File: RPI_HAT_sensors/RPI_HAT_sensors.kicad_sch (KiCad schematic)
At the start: 39 parts, among them J5 Conn_01x01, J6 Conn_01x01

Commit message: h
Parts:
- RV1, RV2: value R_Potentiometer -> 10k
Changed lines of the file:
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@@
     (pin "1")
   )
-  (symbol (lib_id "Connector_Generic:Conn_01x01") (at 355.6 128.27 270) (unit 1)
-    (in_bom yes) (on_board yes) (fields_autoplaced)
-    (property "Reference" "J5" (id 0) (at 358.14 126.9999 90)
-      (effects (font (size 1.27 1.27)) (justify left))
-    )
-    (property "Value" "Conn_01x01" (id 1) (at 358.14 129.5399 90)
-      (effects (font (size 1.27 1.27)) (justify left))
-    )
-    (property "Footprint" "Connector_PinHeader_2.54mm:PinHeader_1x01_P2.54mm_Vertical" (id 2) (at 355.6 128.27 0)
-      (effects (font (size 1.27 1.27)) hide)
-    )
-    (property "Datasheet" "~" (id 3) (at 355.6 128.27 0)
-      (effects (font (size 1.27 1.27)) hide)
-    )
-    (pin "1")
-  )
-  (symbol (lib_id "Device:R_Potentiometer") (at 358.14 77.47 0) (unit 1)
-    (in_bom yes) (on_board yes) (fields_autoplaced)
-    (property "Reference" "RV3" (id 0) (at 355.6 76.1999 0)
-      (effects (font (size 1.27 1.27)) (justify right))
-    )
-    (property "Value" "" (id 1) (at 355.6 78.7399 0)
-      (effects (font (size 1.27 1.27)) (justify right))
-    )
-    (property "Footprint" "" (id 2) (at 358.14 77.47 0)
-      (effects (font (size 1.27 1.27)) hide)
-    )
-    (property "Datasheet" "~" (id 3) (at 358.14 77.47 0)
+  (symbol (lib_id "Device:R_Potentiometer") (at 355.6 116.84 0) (unit 1)
+    (in_bom yes) (on_board yes) (fields_autoplaced)
+    (property "Reference" "RV2" (id 0) (at 353.06 115.5699 0)
+      (effects (font (size 1.27 1.27)) (justify right))
+    )
+    (property "Value" "10k" (id 1) (at 353.06 118.1099 0)
+      (effects (font (size 1.27 1.27)) (justify right))
+    )
+    (property "Footprint" "" (id 2) (at 355.6 116.84 0)
+      (effects (font (size 1.27 1.27)) hide)
+    )
+    (property "Datasheet" "~" (id 3) (at 355.6 116.84 0)
       (effects (font (size 1.27 1.27)) hide)
     )
@@
     (pin "3")
   )
-  (symbol (lib_id "Connector_Generic:Conn_01x01") (at 290.83 128.27 270) (unit 1)
-    (in_bom yes) (on_board yes) (fields_autoplaced)
-    (property "Reference" "J4" (id 0) (at 293.37 126.9999 90)
-      (effects (font (size 1.27 1.27)) (justify left))
-    )
-    (property "Value" "" (id 1) (at 293.37 129.5399 90)
-      (effects (font (size 1.27 1.27)) (justify left))
-    )
-    (property "Footprint" "" (id 2) (at 290.83 128.27 0)
-      (effects (font (size 1.27 1.27)) hide)
-    )
-    (property "Datasheet" "~" (id 3) (at 290.83 128.27 0)
-      (effects (font (size 1.27 1.27)) hide)
-    )
-    (pin "1")
-  )
-  (symbol (lib_id "Device:R_Potentiometer") (at 290.83 116.84 0) (unit 1)
-    (in_bom yes) (on_board yes) (fields_autoplaced)
-    (property "Reference" "RV1" (id 0) (at 288.29 115.5699 0)
-      (effects (font (size 1.27 1.27)) (justify right))
-    )
-    (property "Value" "R_Potentiometer" (id 1) (at 288.29 118.1099 0)
-      (effects (font (size 1.27 1.27)) (justify right))
-    )
-    (property "Footprint" "" (id 2) (at 290.83 116.84 0)
-      (effects (font (size 1.27 1.27)) hide)
-    )
-    (property "Datasheet" "~" (id 3) (at 290.83 116.84 0)
+  (symbol (lib_id "Connector_Generic:Conn_01x01") (at 355.6 128.27 270) (unit 1)
+    (in_bom yes) (on_board yes) (fields_autoplaced)
+    (property "Reference" "J5" (id 0) (at 358.14 126.9999 90)
+      (effects (font (size 1.27 1.27)) (justify left))
+    )
+    (property "Value" "Conn_01x01" (id 1) (at 358.14 129.5399 90)
+      (effects (font (size 1.27 1.27)) (justify left))
+    )
+    (property "Footprint" "Connector_PinHeader_2.54mm:PinHeader_1x01_P2.54mm_Vertical" (id 2) (at 355.6 128.27 0)
+      (effects (font (size 1.27 1.27)) hide)
+    )
+    (property "Datasheet" "~" (id 3) (at 355.6 128.27 0)
+      (effects (font (size 1.27 1.27)) hide)
+    )
+    (pin "1")
+  )
+  (symbol (lib_id "Device:R_Potentiometer") (at 358.14 77.47 0) (unit 1)
+    (in_bom yes) (on_board yes) (fields_autoplaced)
+    (property "Reference" "RV3" (id 0) (at 355.6 76.1999 0)
+      (effects (font (size 1.27 1.27)) (justify right))
+    )
+    (property "Value" "" (id 1) (at 355.6 78.7399 0)
+      (effects (font (size 1.27 1.27)) (justify right))
+    )
+    (property "Footprint" "" (id 2) (at 358.14 77.47 0)
+      (effects (font (size 1.27 1.27)) hide)
+    )
+    (property "Datasheet" "~" (id 3) (at 358.14 77.47 0)
       (effects (font (size 1.27 1.27)) hide)
     )
@@
     (pin "3")
   )
-  (symbol (lib_id "Device:R_Potentiometer") (at 355.6 116.84 0) (unit 1)
-    (in_bom yes) (on_board yes) (fields_autoplaced)
-    (property "Reference" "RV2" (id 0) (at 353.06 115.5699 0)
-      (effects (font (size 1.27 1.27)) (justify right))
-    )
-    (property "Value" "R_Potentiometer" (id 1) (at 353.06 118.1099 0)
-      (effects (font (size 1.27 1.27)) (justify right))
-    )
-    (property "Footprint" "" (id 2) (at 355.6 116.84 0)
-      (effects (font (size 1.27 1.27)) hide)
-    )
-    (property "Datasheet" "~" (id 3) (at 355.6 116.84 0)
+  (symbol (lib_id "Connector_Generic:Conn_01x01") (at 290.83 128.27 270) (unit 1)
+    (in_bom yes) (on_board yes) (fields_autoplaced)
+    (property "Reference" "J4" (id 0) (at 293.37 126.9999 90)
+      (effects (font (size 1.27 1.27)) (justify left))
+    )
+    (property "Value" "" (id 1) (at 293.37 129.5399 90)
+      (effects (font (size 1.27 1.27)) (justify left))
+    )
+    (property "Footprint" "" (id 2) (at 290.83 128.27 0)
+      (effects (font (size 1.27 1.27)) hide)
+    )
+    (property "Datasheet" "~" (id 3) (at 290.83 128.27 0)
+      (effects (font (size 1.27 1.27)) hide)
+    )
+    (pin "1")
+  )
+  (symbol (lib_id "Device:R_Potentiometer") (at 290.83 116.84 0) (unit 1)
+    (in_bom yes) (on_board yes) (fields_autoplaced)
+    (property "Reference" "RV1" (id 0) (at 288.29 115.5699 0)
+      (effects (font (size 1.27 1.27)) (justify right))
+    )
+    (property "Value" "10k" (id 1) (at 288.29 118.1099 0)
+      (effects (font (size 1.27 1.27)) (justify right))
+    )
+    (property "Footprint" "" (id 2) (at 290.83 116.84 0)
+      (effects (font (size 1.27 1.27)) hide)
+    )
+    (property "Datasheet" "~" (id 3) (at 290.83 116.84 0)
       (effects (font (size 1.27 1.27)) hide)
     )
@@
       (reference "R8") (unit 1) (value "3K9") (footprint "Resistor_THT:R_Axial_DIN0204_L3.6mm_D1.6mm_P7.62mm_Horizontal")
     )
-    (path "/ebc401f4-0099-4bec-9a16-490c89dccf91"
-      (reference "RV1") (unit 1) (value "R_Potentiometer") (footprint "")
-    )
-    (path "/f263053c-853e-4bd4-bc1a-6c9983651d47"
-      (reference "RV2") (unit 1) (value "R_Potentiometer") (footprint "")
+    (path "/f4145bdb-e374-4b1f-80c3-57ff67cbefcd"
+      (reference "RV1") (unit 1) (value "10k") (footprint "")
+    )
+    (path "/99095c67-dbe4-40ff-b564-d4764560ce26"
+      (reference "RV2") (unit 1) (value "10k") (footprint "")
     )
     (path "/ae545ba3-9447-46ee-95c9-5c85b1932c57"
-      (reference "RV3") (unit 1) (value "R_Potentiometer") (footprint "")
+      (reference "RV3") (unit 1) (value "10k") (footprint "")
     )
     (path "/00000000-0000-0000-0000-000061c1d53c"

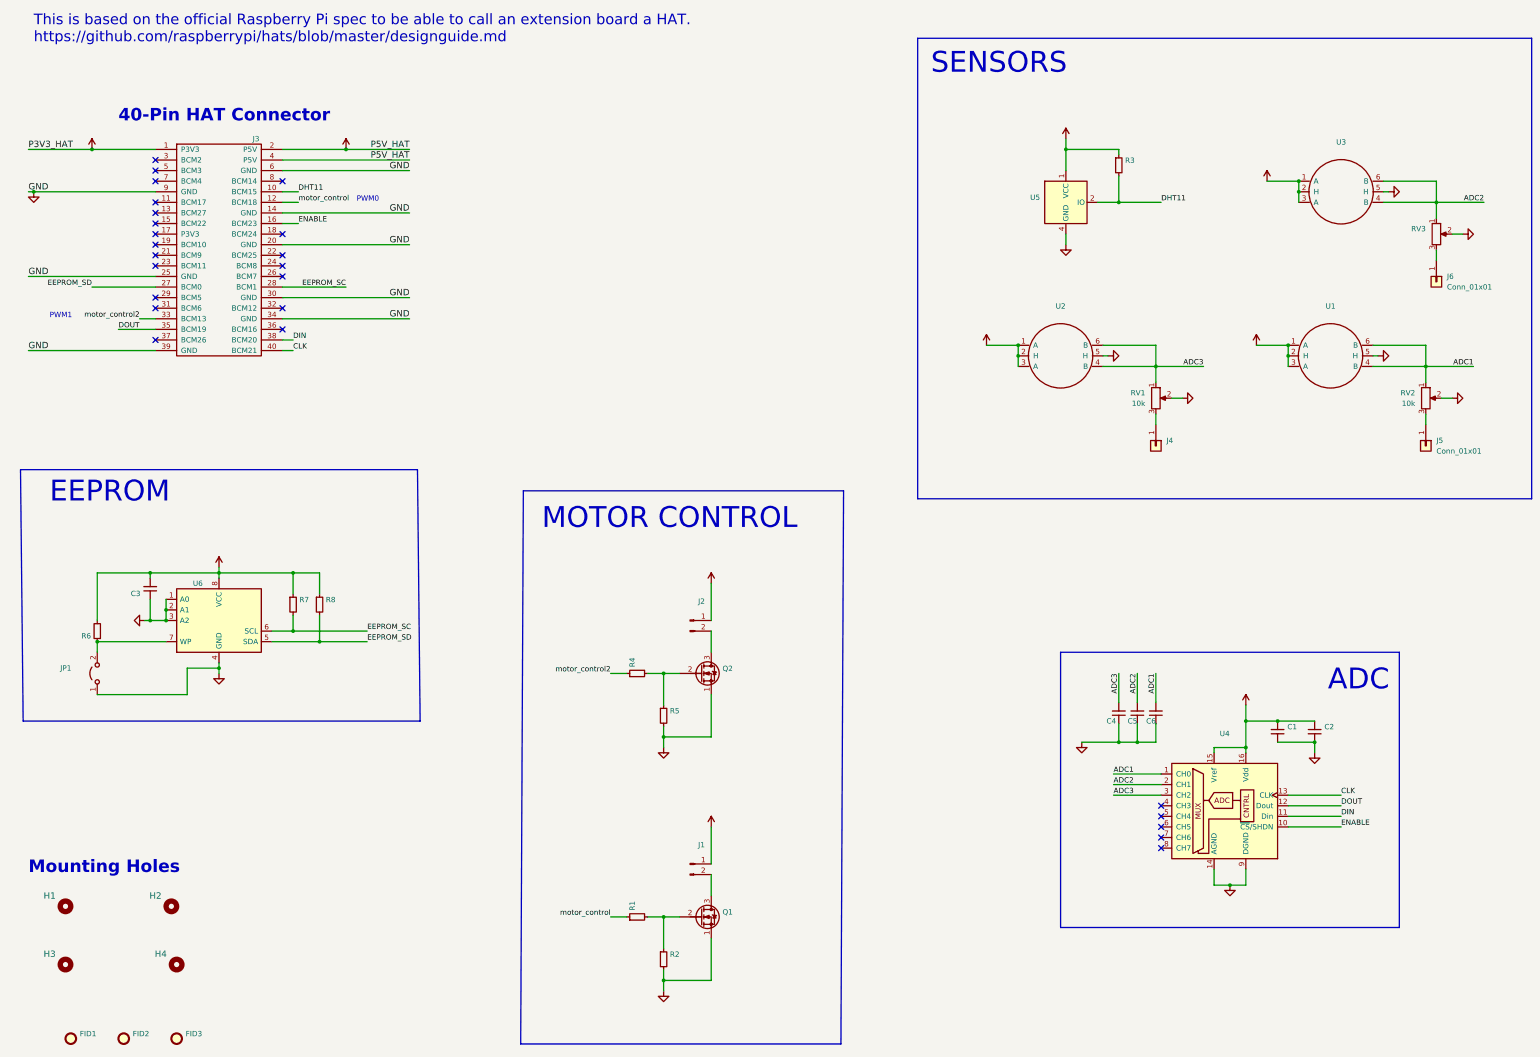
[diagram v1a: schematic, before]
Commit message: Update RPI_HAT_sensors.kicad_sch
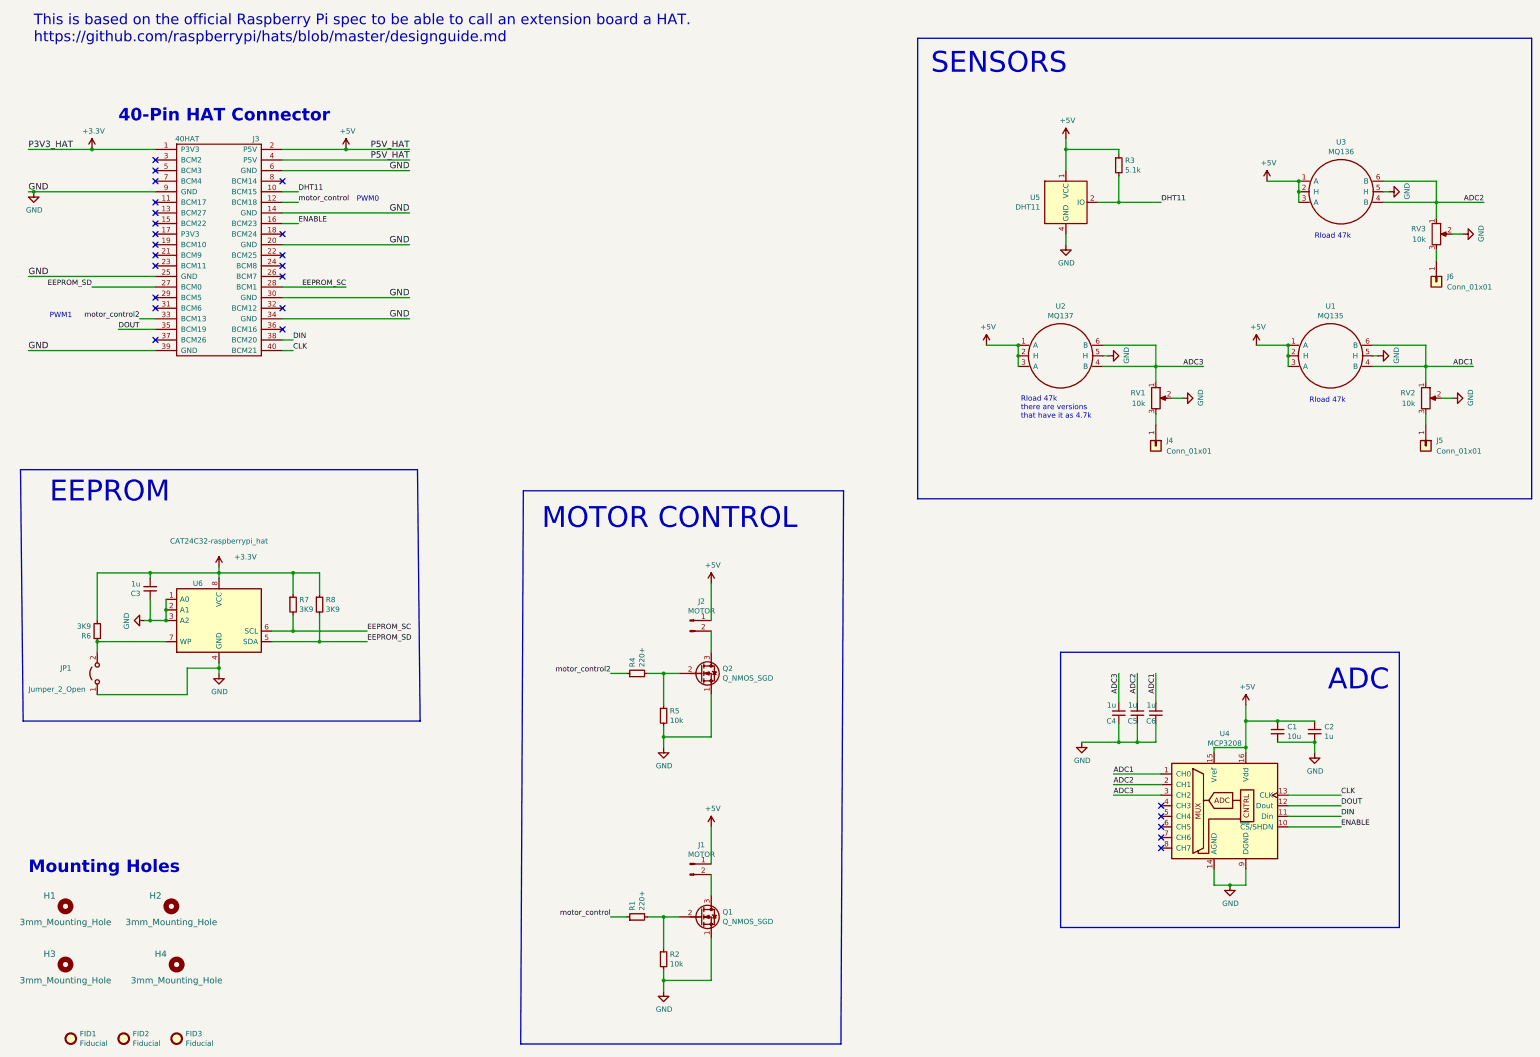
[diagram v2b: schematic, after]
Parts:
- C1: value (none) -> 10u; footprint (none) -> Capacitor_THT:C_Disc_D5.1mm_W3.2mm_P5.00mm
- C2, C3: value (none) -> 1u; footprint (none) -> Capacitor_THT:C_Disc_D5.1mm_W3.2mm_P5.00mm
- C4, C5, C6: value (none) -> 1u; footprint (none) -> Capacitor_SMD:C_0805_2012Metric_Pad1.15x1.40mm_HandSolder
- FID1, FID2, FID3: value (none) -> Fiducial; footprint (none) -> Fiducial:Fiducial_1.5mm_Mask3mm
- H1, H2, H3, H4: value (none) -> 3mm_Mounting_Hole; footprint (none) -> project_footprints:NPTH_3mm_ID
- J1, J2: value (none) -> MOTOR; footprint (none) -> Connector_PinHeader_2.54mm:PinHeader_1x02_P2.54mm_Vertical
- J3: value (none) -> 40HAT; footprint (none) -> Connector_PinSocket_2.54mm:PinSocket_2x20_P2.54mm_Vertical
- J4: value (none) -> Conn_01x01; footprint (none) -> Connector_PinHeader_2.54mm:PinHeader_1x01_P2.54mm_Vertical
- JP1: value (none) -> Jumper_2_Open; footprint (none) -> Connector_PinHeader_2.54mm:PinHeader_1x02_P2.54mm_Vertical
- Q1, Q2: value (none) -> Q_NMOS_SGD; footprint (none) -> Package_TO_SOT_THT:TO-92
- R1, R4: value (none) -> 220+; footprint (none) -> Resistor_THT:R_Axial_DIN0204_L3.6mm_D1.6mm_P7.62mm_Horizontal
- R2, R5: value (none) -> 10k; footprint (none) -> Resistor_THT:R_Axial_DIN0204_L3.6mm_D1.6mm_P7.62mm_Horizontal
- R3: value (none) -> 5.1k; footprint (none) -> Resistor_THT:R_Axial_DIN0204_L3.6mm_D1.6mm_P7.62mm_Horizontal
- R6, R7, R8: value (none) -> 3K9; footprint (none) -> Resistor_THT:R_Axial_DIN0204_L3.6mm_D1.6mm_P7.62mm_Horizontal
- RV3: value (none) -> 10k
- U1: value (none) -> MQ135; footprint (none) -> BEIA_sensors:MQ135
- U2: value (none) -> MQ137; footprint (none) -> BEIA_sensors:MQ135
- U3: value (none) -> MQ136; footprint (none) -> BEIA_sensors:MQ135
- U4: value (none) -> MCP3208; footprint (none) -> Package_DIP:DIP-16_W7.62mm_LongPads
- U5: value (none) -> DHT11; footprint (none) -> Sensor:Aosong_DHT11_5.5x12.0_P2.54mm
- U6: value (none) -> CAT24C32-raspberrypi_hat; footprint (none) -> Package_SO:TSSOP-8_4.4x3mm_P0.65mm
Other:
- note added: "Rload 47k"
- note added: "Rload 47k there are versions that have it as 4.7k"
